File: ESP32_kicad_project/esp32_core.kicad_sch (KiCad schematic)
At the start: 20 parts, among them J1 Conn_01x04_Pin, SW1 SW_Push, SW2 SW_Push, U2 ESP32-WROOM-32E

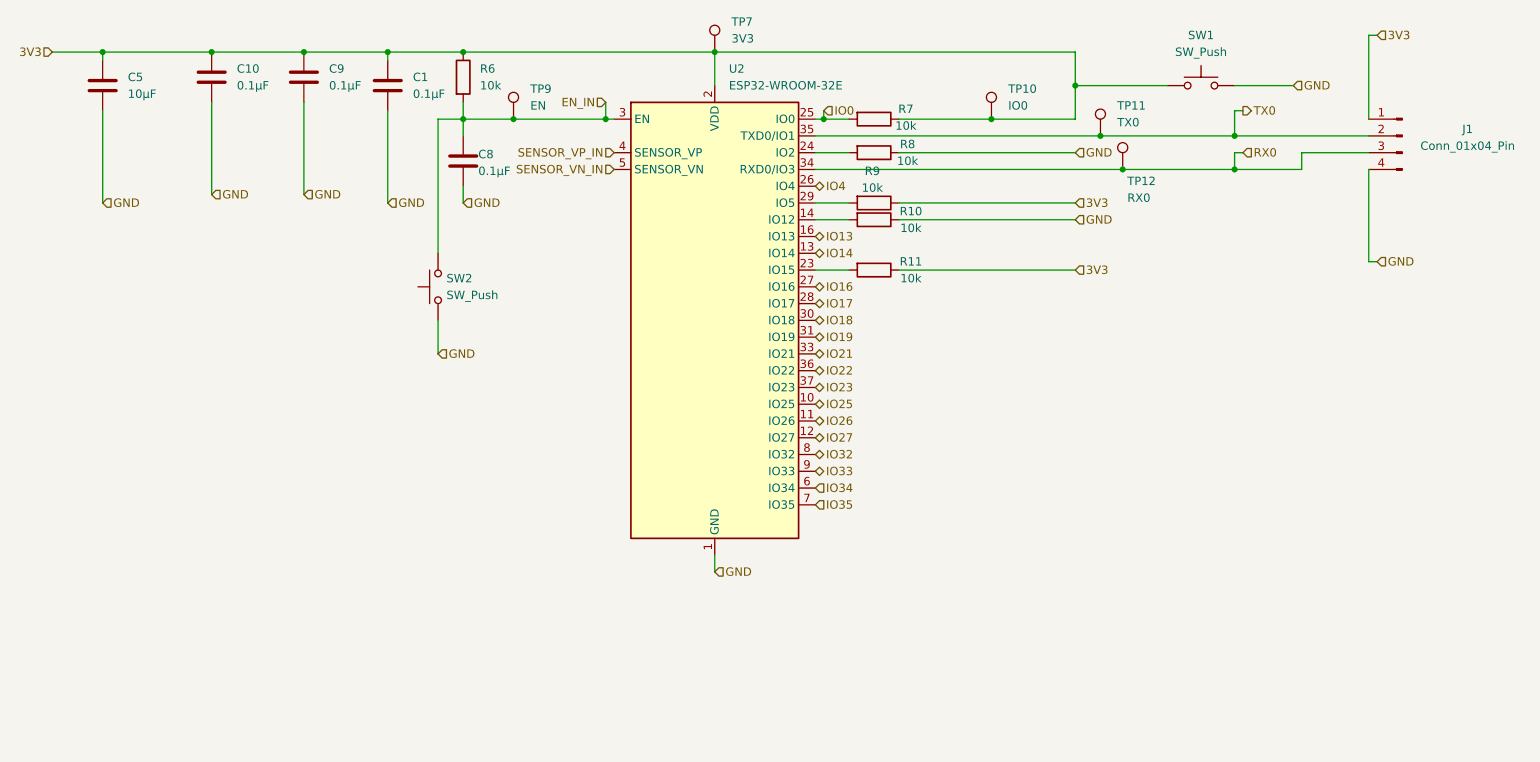
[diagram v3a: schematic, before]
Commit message: added USB chip, implemented ESP32 auto reset DTR RTS circuit
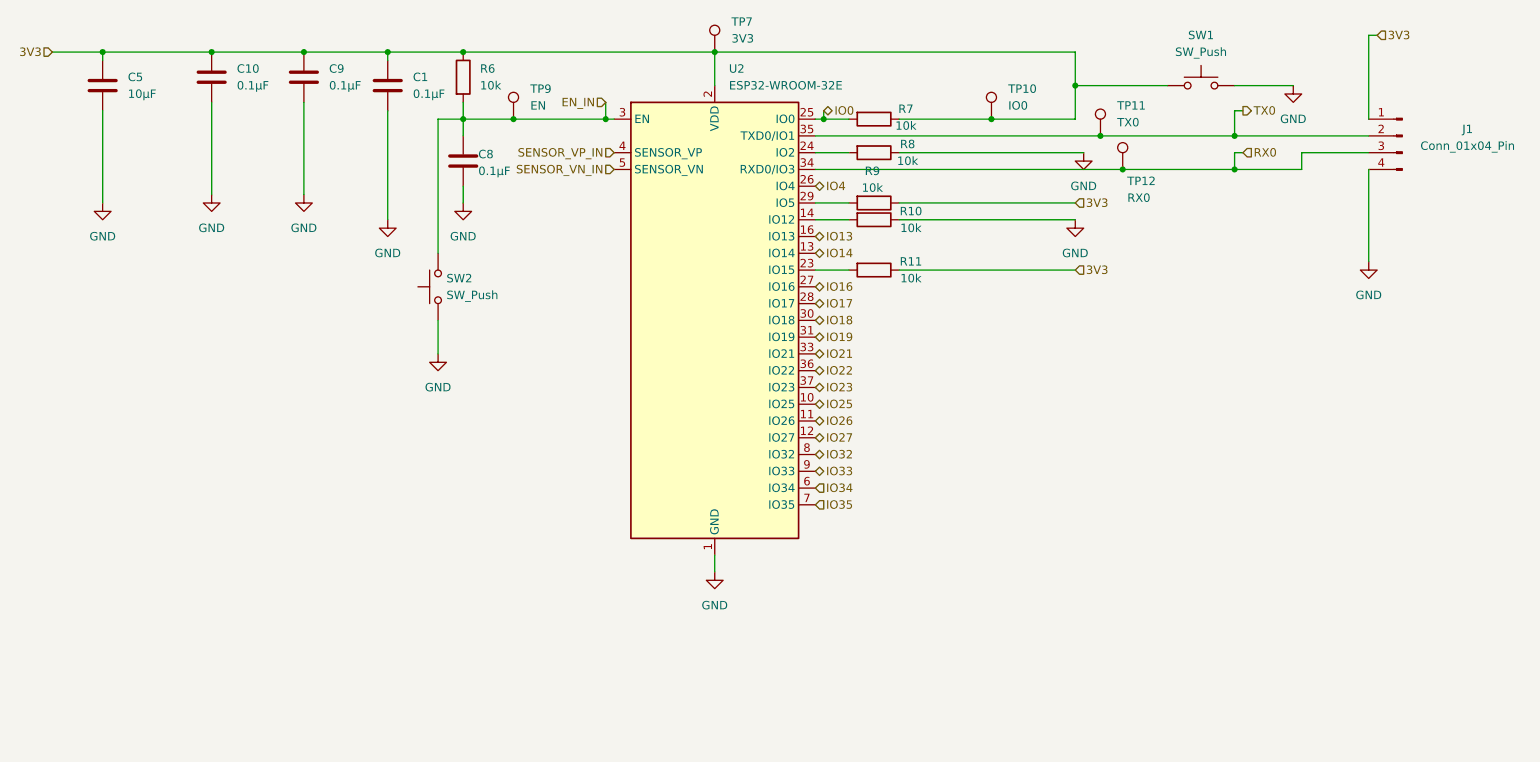
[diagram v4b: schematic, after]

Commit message: completed USB-UART, created GPIO pin connectors, completed schematic work. moving on to PCB
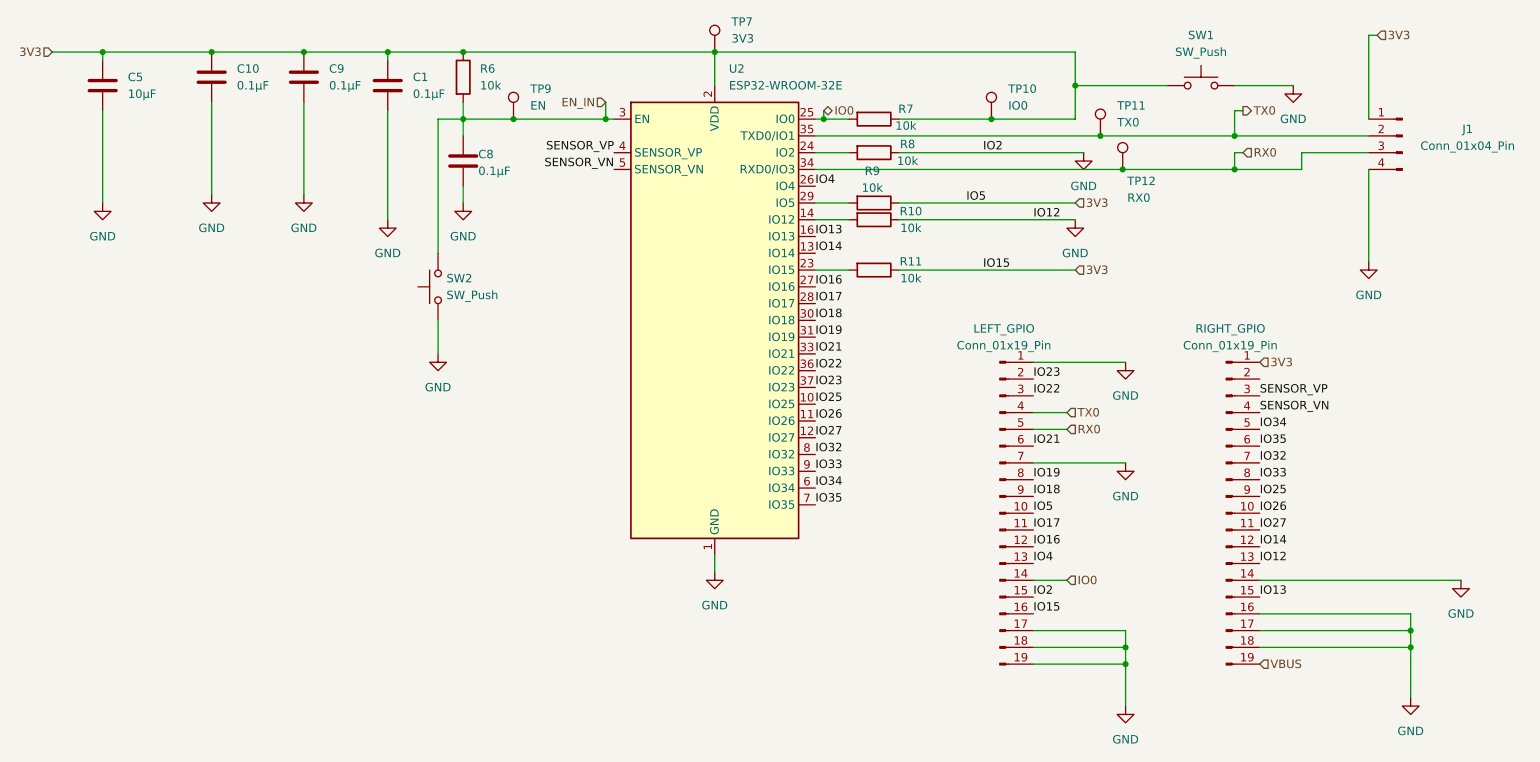
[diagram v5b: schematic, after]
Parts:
- added LEFT_GPIO, RIGHT_GPIO: Conn_01x19_Pin, symbol Connector:Conn_01x19_Pin
- J1: footprint (none) -> Connector_PinHeader_2.54mm:PinHeader_1x04_P2.54mm_Vertical
- SW1, SW2: footprint (none) -> Button_Switch_SMD:SW_SPST_TL3342
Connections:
- net 3V3: now also LEFT_GPIO.10 (Pin_10), LEFT_GPIO.16 (Pin_16), RIGHT_GPIO.1 (Pin_1)
- net GND: now also LEFT_GPIO.1 (Pin_1), LEFT_GPIO.15 (Pin_15), LEFT_GPIO.17 (Pin_17), LEFT_GPIO.18 (Pin_18), LEFT_GPIO.19 (Pin_19), LEFT_GPIO.7 (Pin_7), RIGHT_GPIO.13 (Pin_13), RIGHT_GPIO.14 (Pin_14), RIGHT_GPIO.16 (Pin_16), RIGHT_GPIO.17 (Pin_17), RIGHT_GPIO.18 (Pin_18)
- net IO0: now also LEFT_GPIO.14 (Pin_14)
- net IO13: now also RIGHT_GPIO.15 (Pin_15)
- net IO14: now also RIGHT_GPIO.12 (Pin_12)
- net IO16: now also LEFT_GPIO.12 (Pin_12)
- net IO17: now also LEFT_GPIO.11 (Pin_11)
- net IO18: now also LEFT_GPIO.9 (Pin_9)
- net IO19: now also LEFT_GPIO.8 (Pin_8)
- net IO21: now also LEFT_GPIO.6 (Pin_6)
- net IO22: now also LEFT_GPIO.3 (Pin_3)
- net IO23: now also LEFT_GPIO.2 (Pin_2)
- net IO25: now also RIGHT_GPIO.9 (Pin_9)
- net IO26: now also RIGHT_GPIO.10 (Pin_10)
- net IO27: now also RIGHT_GPIO.11 (Pin_11)
- net IO32: now also RIGHT_GPIO.7 (Pin_7)
- net IO33: now also RIGHT_GPIO.8 (Pin_8)
- net IO34: now also RIGHT_GPIO.5 (Pin_5)
- net IO35: now also RIGHT_GPIO.6 (Pin_6)
- net IO4: now also LEFT_GPIO.13 (Pin_13)
- net RX0: now also LEFT_GPIO.5 (Pin_5)
- net TX0: now also LEFT_GPIO.4 (Pin_4)
- net SENSOR_VN_IN renamed SENSOR_VN
- net SENSOR_VN: now also RIGHT_GPIO.4 (Pin_4)
- net SENSOR_VP_IN renamed SENSOR_VP
- net SENSOR_VP: now also RIGHT_GPIO.3 (Pin_3)
- new net VBUS: RIGHT_GPIO.19 (Pin_19)

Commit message: completed schematic design, replaced regulator output inductor with a smaller part, fit components in a board in PCB editor, will start routing
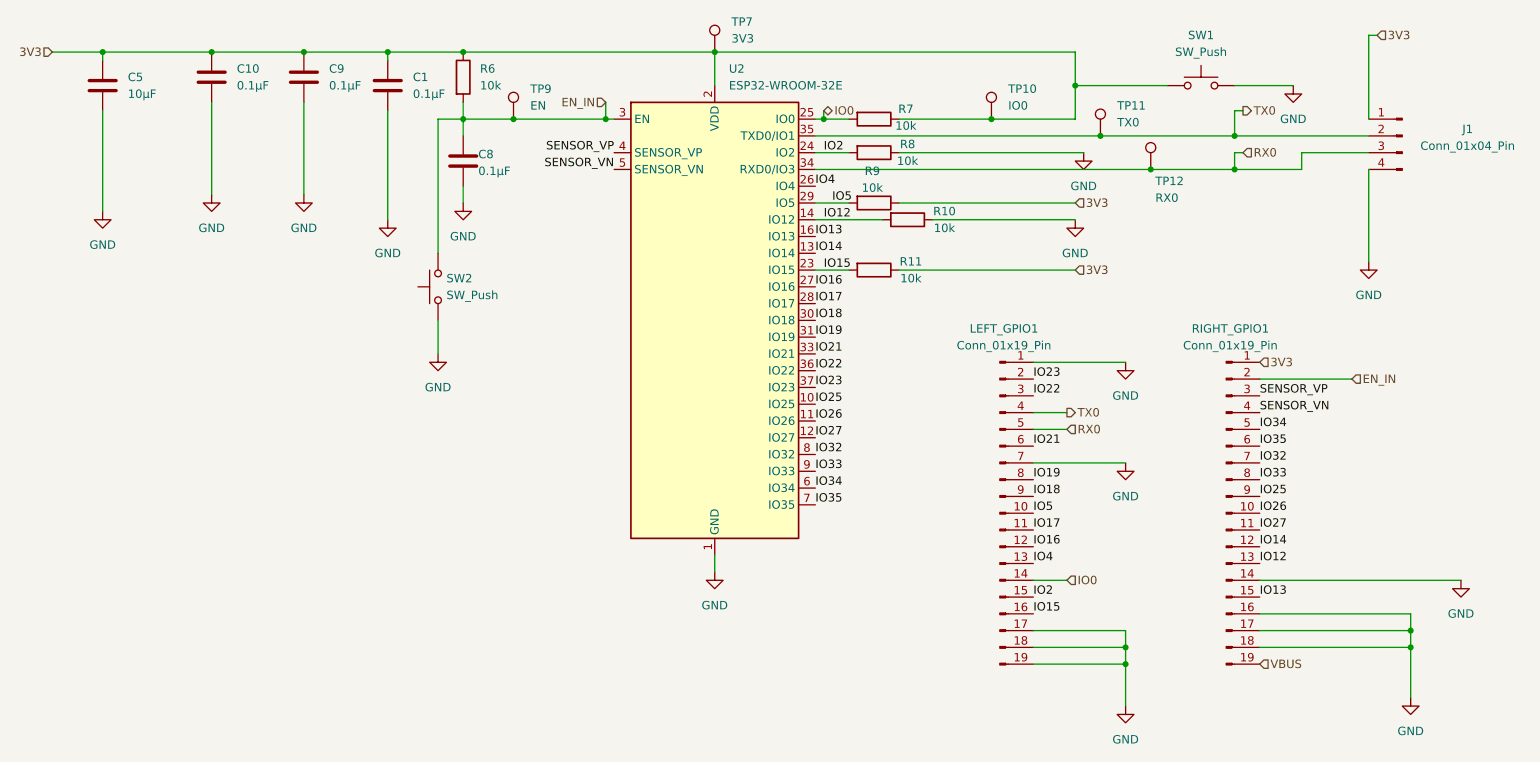
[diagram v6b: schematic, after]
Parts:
- LEFT_GPIO1: renamed from LEFT_GPIO; footprint (none) -> Connector_PinHeader_1.27mm:PinHeader_1x19_P1.27mm_Vertical
- RIGHT_GPIO1: renamed from RIGHT_GPIO; footprint (none) -> Connector_PinHeader_1.27mm:PinHeader_1x19_P1.27mm_Vertical
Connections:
- net 3V3: no longer LEFT_GPIO1.10 (Pin_10), LEFT_GPIO1.16 (Pin_16)
- net EN_IN: now also RIGHT_GPIO1.2 (Pin_2)
- net GND: no longer LEFT_GPIO1.15 (Pin_15), RIGHT_GPIO1.13 (Pin_13)
- net IO12: now reaches R10.2, U2.14 (IO12)
- net IO12: now also RIGHT_GPIO1.13 (Pin_13)
- net IO5: now reaches R9.2, U2.29 (IO5)
- net IO5: now also LEFT_GPIO1.10 (Pin_10)
- net IO15: now reaches R11.2, U2.23 (IO15)
- net IO15: now also LEFT_GPIO1.16 (Pin_16)
- net IO2: now reaches R8.2, U2.24 (IO2)
- net IO2: now also LEFT_GPIO1.15 (Pin_15)
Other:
- moved on the sheet: R10, TP12
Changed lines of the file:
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@@
 	)
 	(junction
+		(at 193.04 73.66)
+		(diameter 0)
+		(color 0 0 0 0)
+	)
+	(junction
 		(at 189.23 148.59)
 		(diameter 0)
@@
 	)
 	(junction
-		(at 188.7936 73.66)
-		(diameter 0)
-		(color 0 0 0 0)
-	)
-	(junction
 		(at 127 55.88)
 		(diameter 0)
@@
 	(wire
 		(pts
-			(xy 188.7936 73.66) (xy 142.24 73.66)
+			(xy 142.24 73.66) (xy 193.04 73.66)
 		)
 		(stroke
@@
 	(wire
 		(pts
-			(xy 154.94 81.28) (xy 181.61 81.28)
+			(xy 160.02 81.28) (xy 181.61 81.28)
 		)
 		(stroke
@@
 	(wire
 		(pts
+			(xy 223.52 105.41) (xy 209.55 105.41)
+		)
+		(stroke
+			(width 0)
+			(type default)
+		)
+	)
+	(wire
+		(pts
 			(xy 181.61 60.96) (xy 181.61 55.88)
 		)
@@
 	(wire
 		(pts
-			(xy 142.24 81.28) (xy 147.32 81.28)
+			(xy 142.24 81.28) (xy 152.4 81.28)
 		)
 		(stroke
@@
 	(wire
 		(pts
-			(xy 205.74 73.66) (xy 188.7936 73.66)
-		)
-		(stroke
-			(width 0)
-			(type default)
-		)
-	)
-	(wire
-		(pts
 			(xy 175.26 148.59) (xy 189.23 148.59)
 		)
@@
 	(wire
 		(pts
-			(xy 34.29 64.77) (xy 34.29 78.74)
+			(xy 34.29 64.77) (xy 34.29 80.01)
 		)
 		(stroke
@@
 	(wire
 		(pts
+			(xy 193.04 73.66) (xy 205.74 73.66)
+		)
+		(stroke
+			(width 0)
+			(type default)
+		)
+	)
+	(wire
+		(pts
 			(xy 50.8 55.88) (xy 64.77 55.88)
 		)
@@
 	(wire
 		(pts
-			(xy 85.09 86.36) (xy 85.09 66.04)
+			(xy 154.94 71.12) (xy 182.88 71.12)
 		)
 		(stroke
@@
 	(wire
 		(pts
-			(xy 168.91 66.04) (xy 181.61 66.04)
+			(xy 85.09 86.36) (xy 85.09 66.04)
 		)
 		(stroke
@@
 	(wire
 		(pts
-			(xy 181.61 66.04) (xy 181.61 60.96)
+			(xy 168.91 66.04) (xy 181.61 66.04)
 		)
 		(stroke
@@
 	(wire
 		(pts
-			(xy 240.03 135.89) (xy 209.55 135.89)
+			(xy 181.61 66.04) (xy 181.61 60.96)
 		)
 		(stroke
@@
 	(wire
 		(pts
-			(xy 142.24 88.9) (xy 147.32 88.9)
+			(xy 240.03 135.89) (xy 209.55 135.89)
 		)
 		(stroke
@@
 	(wire
 		(pts
-			(xy 232.41 146.05) (xy 232.41 143.51)
+			(xy 142.24 88.9) (xy 147.32 88.9)
 		)
 		(stroke
@@
 	(wire
 		(pts
-			(xy 77.47 55.88) (xy 77.47 57.15)
+			(xy 232.41 146.05) (xy 232.41 143.51)
 		)
 		(stroke
@@
 	(wire
 		(pts
-			(xy 154.94 71.12) (xy 182.88 71.12)
+			(xy 77.47 55.88) (xy 77.47 57.15)
 		)
 		(stroke
@@
 	)
 	(label "IO12"
-		(at 175.26 81.28 0)
+		(at 143.51 81.28 0)
 		(effects
 			(font
@@
 	)
 	(label "IO5"
-		(at 165.1 78.74 0)
+		(at 144.78 78.74 0)
 		(effects
 			(font
@@
 	)
 	(label "IO2"
-		(at 167.64 71.12 0)
+		(at 143.51 71.12 0)
 		(effects
 			(font
@@
 	)
 	(label "IO15"
-		(at 167.64 88.9 0)
+		(at 143.51 88.9 0)
 		(effects
 			(font
@@
 	)
 	(hierarchical_label "TX0"
-		(shape input)
+		(shape output)
 		(at 180.34 110.49 0)
 		(effects
@@
 		)
 	)
+	(hierarchical_label "EN_IN"
+		(shape input)
+		(at 223.52 105.41 0)
+		(effects
+			(font
+				(size 1.27 1.27)
+			)
+			(justify left)
+		)
+	)
 	(hierarchical_label "3V3"
 		(shape input)
@@
 	(symbol
 		(lib_id "power:GND")
-		(at 34.29 78.74 0)
+		(at 34.29 80.01 0)
 		(unit 1)
 		(exclude_from_sim no)
@@
 		(fields_autoplaced yes)
 		(property "Reference" "#PWR013"
-			(at 34.29 85.09 0)
+			(at 34.29 86.36 0)
 			(effects
 				(font
@@
 		)
 		(property "Value" "GND"
-			(at 34.29 83.82 0)
+			(at 34.29 85.09 0)
 			(effects
 				(font
@@
 		)
 		(property "Footprint" ""
-			(at 34.29 78.74 0)
+			(at 34.29 80.01 0)
 			(effects
 				(font
@@
 		)
 		(property "Datasheet" ""
-			(at 34.29 78.74 0)
+			(at 34.29 80.01 0)
 			(effects
 				(font
@@
 		)
 		(property "Description" "Power symbol creates a global label with name \"GND\" , ground"
-			(at 34.29 78.74 0)
+			(at 34.29 80.01 0)
 			(effects
 				(font
@@
 	(symbol
 		(lib_id "Device:R")
-		(at 151.13 81.28 270)
+		(at 156.21 81.28 270)
 		(unit 1)
 		(exclude_from_sim no)
@@
 		(dnp no)
 		(property "Reference" "R10"
-			(at 156.718 80.01 90)
+			(at 161.798 80.01 90)
 			(effects
 				(font
@@
 		)
 		(property "Value" "10k"
-			(at 156.718 82.55 90)
+			(at 161.798 82.55 90)
 			(effects
 				(font
@@
 		)
 		(property "Footprint" "Resistor_SMD:R_0603_1608Metric"
-			(at 151.13 79.502 90)
+			(at 156.21 79.502 90)
 			(effects
 				(font
@@
 		)
 		(property "Datasheet" "~"
-			(at 151.13 81.28 0)
+			(at 156.21 81.28 0)
 			(effects
 				(font
@@
 		)
 		(property "Description" "Resistor"
-			(at 151.13 81.28 0)
+			(at 156.21 81.28 0)
 			(effects
 				(font
@@
 		(dnp no)
 		(fields_autoplaced yes)
-		(property "Reference" "LEFT_GPIO"
+		(property "Reference" "LEFT_GPIO1"
 			(at 170.815 97.79 0)
 			(effects
@@
 			)
 		)
-		(property "Footprint" ""
+		(property "Footprint" "Connector_PinHeader_1.27mm:PinHeader_1x19_P1.27mm_Vertical"
 			(at 170.18 125.73 0)
 			(effects
@@
 			(project ""
 				(path "/8f7d6ecf-e535-4443-9266-fe4b2e9314d5/71ad0a68-ebcc-403d-8fb5-019c32511765"
-					(reference "LEFT_GPIO")
+					(reference "LEFT_GPIO1")
 					(unit 1)
 				)
@@
 	(symbol
 		(lib_id "Connector:TestPoint")
-		(at 188.7936 73.66 0)
+		(at 193.04 73.66 0)
 		(unit 1)
 		(exclude_from_sim no)
@@
 		(dnp no)
 		(property "Reference" "TP12"
-			(at 189.484 75.438 0)
+			(at 193.7304 75.438 0)
 			(effects
 				(font
@@
 		)
 		(property "Value" "RX0"
-			(at 189.484 77.978 0)
+			(at 193.7304 77.978 0)
 			(effects
 				(font
@@
 		)
 		(property "Footprint" "TestPoint:TestPoint_Pad_D1.5mm"
-			(at 193.8736 73.66 0)
+			(at 198.12 73.66 0)
 			(effects
 				(font
@@
 		)
 		(property "Datasheet" "~"
-			(at 193.8736 73.66 0)
+			(at 198.12 73.66 0)
 			(effects
 				(font
@@
 		)
 		(property "Description" "test point"
-			(at 188.7936 73.66 0)
+			(at 193.04 73.66 0)
 			(effects
 				(font
@@
 		(dnp no)
 		(fields_autoplaced yes)
-		(property "Reference" "RIGHT_GPIO"
+		(property "Reference" "RIGHT_GPIO1"
 			(at 205.105 97.79 0)
 			(effects
@@
 			)
 		)
-		(property "Footprint" ""
+		(property "Footprint" "Connector_PinHeader_1.27mm:PinHeader_1x19_P1.27mm_Vertical"
 			(at 204.47 125.73 0)
 			(effects
@@
 			(project "ESP32_kicad_project"
 				(path "/8f7d6ecf-e535-4443-9266-fe4b2e9314d5/71ad0a68-ebcc-403d-8fb5-019c32511765"
-					(reference "RIGHT_GPIO")
+					(reference "RIGHT_GPIO1")
 					(unit 1)
 				)

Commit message: routed the regulator properly, VBUS and 3V3 are also routed
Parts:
- J1: footprint Connector_PinHeader_2.54mm:PinHeader_1x04_P2.54mm_Vertical -> Connector_PinHeader_1.27mm:PinHeader_1x04_P1.27mm_Vertical
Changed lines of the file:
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@@
 			)
 		)
-		(property "Footprint" "Connector_PinHeader_2.54mm:PinHeader_1x04_P2.54mm_Vertical"
+		(property "Footprint" "Connector_PinHeader_1.27mm:PinHeader_1x04_P1.27mm_Vertical"
 			(at 231.14 68.58 0)
 			(effects
